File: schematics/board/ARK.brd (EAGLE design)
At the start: 82 x 92 mm, 85 parts, among them IC2 STM32F103C8T

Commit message: Готова схема платы АРК
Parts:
- removed 3,3µH: 3,3µ, CanCubeSat:B82472G6
- removed 3,3µH1: 3,3µH, CanCubeSat:B82472G6
- removed AD5272#2: AD5272, CanCubeSat:MSOP10
- removed C29: 1µ, rcl:C0603
- removed C3: 470nF, rcl:C0603
- removed C40, C41, C49, C50, C56: 0,1µ, rcl:C0603
- removed C44, C52: 680p, rcl:C0603
- removed C45, C53: 4.7µ, rcl:C1206
- removed C46: 3,3n, rcl:C0603
- removed C47, C54: 150µ, CanCubeSat:ECAP150-CMD
- removed C48, C55: 220µ, CanCubeSat:ECAP220-CMD
- removed C57: 10µ, rcl:C1206
- removed INVERT: INVERTER., CanCubeSat:SC70
- removed LED_G1, LED_G2, LED_R1, LED_R2: (no value), led:CHIPLED_0603
- removed OPA: OPA333, CanCubeSat:SOT23-5
- removed R1: 91K, resistor:R0603
- removed R100, R32, R33, R57: 2k, resistor:R0603
- removed R28, R30, R67, R68, R69: 150k, resistor:R0603
- removed R3: 14K3, resistor:R0603
- removed R4: 120k, resistor:R0603
- removed R5: 430k, resistor:R0603
- removed R65: 1M, resistor:R0603
- removed R66: 10k, resistor:R0603
- removed R7: 680k, resistor:R0603
- removed REF3033: REF3033, CanCubeSat:SOT23-3
- removed U$1: MF-R400, CanCubeSat:MF-R400
- removed U$23, U$59: LTC31191, CanCubeSat:LTC3119+VIA
- removed VR-FB: 3314G-1-504E, CanCubeSat:TRIM_3314G-1-504E
- removed VR-RUN: 3313J-1-205E, CanCubeSat:TRIM_3313J-1-205E
- added 3362H, 3362H1: 20k, CanCubeSat:TRIM_3362H
- added 3362P, 3362P1, 3362P4: 1k, CanCubeSat:TRIM_3362P-1-502LF
- added 3362P2, 3362P5: 5k, CanCubeSat:TRIM_3362P-1-502LF
- added 3362P3: 500R, CanCubeSat:TRIM_3362P-1-502LF
- added C1.C, C1.D, C2B.C, C2B.D: 100nF, rcl:C0603
- added C2A.C, C2A.D: 22µF, rcl:C1206
- added C3.C, C3.D, C4A.C, C4A.D, C5.C, C5.D: 1µF, rcl:C0603
- added C4B.C, C4B.D: 1000µF, CanCubeSat:ECAP1000-CMD
- added C6.C, C6.D: 10nF, rcl:C0603
- added C7.C, C7.D, C8.C, C8.D: (10nF), rcl:C0603
- added INVERT1: INVERTER., CanCubeSat:SC70
- added L1.C, L1.D: 10µH, CanCubeSat:L_12X12
- added OPA1, OPA2, OPA3: OPA333, CanCubeSat:SOT23-5
- added PB1, PB2, PB3, PB4, PB6, PB7: (no value), led:CHIPLED_0603
- added R1.C, R1.D: 62k, rcl:R0603
- added R10, R12, R14, R15, R2, R21, R25, R29, R31, R34, R35, R36, R37, R38, R39, R40, R41, R42, R45, R48, R49, R6, R8, R9: 10k, resistor:R0603
- added R10.C, R10.D: 11k, rcl:R0603
- added R11: 34k8, resistor:R0603
- added R11.C, R11.D, R12.C, R12.D, R13.C, R13.D, R14.C, R14.D, R15.C, R15.D: 100k, rcl:R0603
- added R13: 91k, resistor:R0603
- added R16, R17, R18, R22, R23, R24, R26, R43: 2k, resistor:R0603
- added R16.C, R16.D, R17.C, R17.D, R2.C, R2.D, R6.C, R6.D: 10k, rcl:R0603
- added R18.C, R18.D: 51k, rcl:R0603
- added R19, R20: 51k, resistor:R0603
- added R19.C, R19.D: (1M), rcl:R0603
- added R44: 1k, resistor:R0603
- added R46: 24k9, resistor:R0603
- added R47: 620k, resistor:R0603
- added R5.C, R5.D: 191k, rcl:R0603
- added R7.C, R7.D: 17k8, rcl:R0603
- added R8.C, R8.D: (10k), rcl:R0603
- added R9.C, R9.D: 200k, rcl:R0603
- added ROZE1, ROZE2, ROZE3, ROZE4: (no value), pinheadCS:1X02
- added U$10, U$11, U$17, U$18, U$19, U$22, U$24, U$25, U$27, U$28, U$30, U$31, U$32, U$33, U$41, U$42, U$43, U$46, U$47, U$48, U$50, U$51, U$53, U$9: VIAS, CanCubeSat:VIAS
- added U$13, U$14, U$15, U$16, U$20, U$21, U$26, U$29, U$39, U$40, U$44, U$45, U$49, U$52: VIAS-CONNECT, CanCubeSat:VIAS-CONNECT
- added U$2, U$5: MP5515, CanCubeSat:QFN-30
- added U$34, U$35, U$6: IRF7329PBF, CanCubeSat:SO8
- added U$36, U$37: IRF7905PBF, CanCubeSat:SO8
- added U$38: SI2302CDS, CanCubeSat:SOT23-3
- added U$7, U$8: SMP100LC-8, CanCubeSat:SMB
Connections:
- removed net 3V3-STAB: IC2.9, INVERT.P$5, OPA.P$5, R4.1, REF3033.2
- removed net 90: R65.1, R66.2, R67.2, U$59.15
- removed net DPD_RST: AD5272#2.7, IC2.28
- removed net GND-OUT: JP1.11, JP1.12, U$1.P$2, U$12.P$3, U$12.P$5, U$12.P$7, U$12.P$9
- removed net N$129: C41.2, U$59.3
- removed net N$131: 3,3µH.2, C40.1, U$59.21, U$59.24
- removed net N$132: 3,3µH.1, C41.1, U$59.5, U$59.8
- removed net N$135: R69.1, U$59.13
- removed net N$136: C44.1, R69.2
- removed net N$139: C46.1, R66.1
- removed net N$142: R68.2, U$59.17
- removed net N$144: C40.2, U$59.26
- removed net N$161: IC2.41, R81.1
- removed net N$2: OPA.P$3, R4.2, R5.2, R7.2
- removed net N$215: AD5272#2.1, C53.1, C56.1, C57.1, LED_G2.A, U$23.11, U$23.15, U$23.16
- removed net N$234: C45.1, LED_G1.A, U$59.11, U$59.16
- removed net N$3: AD5272#2.2, R1.2, U$23.12
- removed net N$48: AD5272#2.3, AD5272#2.4, C29.2, R3.1
- removed net N$51: AD5272#2.5, C29.1
- removed net N$77: 3,3µH1.2, C49.1, U$23.21, U$23.24
- removed net N$78: 3,3µH1.1, C50.1, U$23.5, U$23.8
- removed net N$79: R28.2, U$23.17
- removed net N$80: C49.2, U$23.26
- removed net N$81: R30.1, U$23.13
- removed net N$82: C52.1, R30.2
- removed net N$84: C50.2, U$23.3
- removed net N$85: LED_R1.A, R32.2
- removed net N$87: LED_R2.A, R57.2
- removed net N$89: U$59.12, VR-FB.2
- removed net N$91: LED_G1.C, R100.2
- removed net N$92: LED_G2.C, R33.2
- removed net PGOOD1: IC2.19, LED_R2.C, U$59.10
- removed net PGOOD2: IC2.18, LED_R1.C, U$23.10
- removed net RUN: OPA.P$4, VR-RUN.2
- new net 0V8: 3362P.2, OPA2.P$3, U$32.P$1
- new net AGND: C1.C.1, C1.D.1, C3.C.2, C3.D.2, C6.C.2, C6.D.2, C7.C.2, C7.D.2, C8.C.2, C8.D.2, R10.C.2, R10.D.2, R13.C.1, R13.D.1, R18.C.2, R18.D.2, R19.C.2, R19.D.2, R2.C.2, R2.D.2, R6.C.2, R6.D.2, R7.C.1, R7.D.1, U$2.9, U$39.2, U$5.9
- new net DC-DC: IC2.38, R42.2, U$38.1
- new net FBB-C: R15.2, U$2.22
- new net FBB-D: R25.2, U$5.22
- new net INT-C: IC2.40, R15.C.1, U$2.17
- new net INT-D: IC2.29, R15.D.1, U$5.17
- new net LED: IC2.18, R81.1
- new net N$10: R1.C.2, R2.C.1, U$2.10
- new net N$100: 3362P5.2, OPA1.P$4, U$48.P$1
- new net N$101: R45.2, U$44.1, U$47.P$1
- new net N$102: R46.1, U$45.2, U$46.P$1
- new net N$104: 3362H1.1, R48.1
- new net N$105: 3362H1.2, OPA1.P$3, U$51.P$1
- new net N$106: 3362H1.3, R47.2
- new net N$108: R47.1, U$49.2, U$50.P$1
- new net N$109: R48.2, U$52.2, U$53.P$1
- new net N$11: R10.C.1, R9.C.2, U$2.4
- new net N$12: C8.C.1, U$2.7
- new net N$13: R18.C.1, U$2.21
- new net N$15: R19.C.1, U$2.20
- new net N$16: R13.C.2, U$2.5
- new net N$18: C6.C.1, U$2.1
- new net N$19: C4A.C.2, C4B.C.P$1, R5.C.1, R8.C.1, U$2.26
- new net N$20: C5.C.2, U$2.25
- new net N$21: C5.C.1, L1.C.P$1, U$2.27
- new net N$22: R5.C.2, R6.C.1, U$2.23
- new net N$23: R8.C.2, U$2.24
- new net N$24: 3362P4.1, R22.1
- new net N$25: R29.2, U$36.7, U$36.8, U$6.4
- new net N$26: R17.C.1, U$2.19
- new net N$27: R16.C.1, U$2.18
- new net N$28: R35.2, U$34.2, U$37.5, U$37.6
- new net N$29: 3362P2.2, OPA3.P$3, U$19.P$1
- new net N$30: R11.D.1, R12.D.2, U$5.13
- new net N$31: R1.D.2, R2.D.1, U$5.10
- new net N$32: R10.D.1, R9.D.2, U$5.4
- new net N$33: R7.D.2, U$5.8
- new net N$34: C7.D.1, U$5.3
- new net N$35: C8.D.1, U$5.7
- new net N$36: R18.D.1, U$5.21
- new net N$37: R19.D.1, U$5.20
- new net N$38: R13.D.2, U$5.5
- new net N$39: C6.D.1, U$5.1
- new net N$40: C5.D.2, U$5.25
- new net N$41: C5.D.1, L1.D.P$1, U$5.27
- new net N$42: R5.D.2, R6.D.1, U$5.23
- new net N$43: R8.D.2, U$5.24
- new net N$44: C4A.D.2, C4B.D.P$1, R5.D.1, R8.D.1, U$5.26
- new net N$46: U$35.5, U$35.6, U$35.7, U$35.8
- new net N$47: R17.D.1, U$5.19
- new net N$49: R16.D.1, U$5.18
- new net N$5: R34.2, U$34.4, U$37.7, U$37.8
- new net N$52: OPA2.P$1, R15.1, U$29.1
- new net N$53: 3362H.2, OPA2.P$4, U$28.P$1
- new net N$54: 3362H.3, R9.2
- new net N$55: 3362H.1, R10.1
- new net N$56: PB1.C, R16.2
- new net N$57: 3362P.3, R11.1
- new net N$58: 3362P.1, R12.2
- new net N$59: 3362P1.3, R13.1
- new net N$6: OPA3.P$1, R25.1, U$13.1
- new net N$60: 3362P1.1, R14.2
- new net N$61: 3362P1.2, U$25.P$1, U$26.1
- new net N$62: 3362P2.3, R20.1
- new net N$63: PB2.C, R17.2
- new net N$64: 3362P2.1, R21.2
- new net N$65: PB3.C, R18.2
- new net N$66: 3362P4.2, OPA3.P$4, U$10.P$1
- new net N$67: 3362P4.3, R19.2
- new net N$68: PB4.C, R23.2
- new net N$69: PB6.C, R24.2
- new net N$7: R11.C.1, R12.C.2, U$2.13
- new net N$70: PB7.C, R26.2
- new net N$71: R22.2, U$13.2, U$9.P$1
- new net N$72: R19.1, U$11.P$1, U$14.2
- new net N$73: R20.2, U$15.1, U$18.P$1
- new net N$74: R21.1, U$16.2, U$17.P$1
- new net N$75: R13.2, U$21.2, U$24.P$1
- new net N$76: R14.1, U$20.1, U$22.P$1
- new net N$8: R7.C.2, U$2.8
- new net N$83: R9.1, U$26.2, U$27.P$1
- new net N$86: R10.2, U$29.2, U$30.P$1
- new net N$88: R31.2, U$36.5, U$36.6, U$6.2
- new net N$9: C7.C.1, U$2.3
- new net N$90: 3362P3.3, R43.1
- new net N$93: 3362P3.1, R44.2
- new net N$94: 3362P3.2, U$43.P$1, U$52.1
- new net N$95: R40.2, R41.2, U$35.2, U$35.4, U$38.3
- new net N$96: R43.2, U$39.1, U$42.P$1
- new net N$97: R44.1, U$40.2, U$41.P$1
- new net N$98: 3362P5.3, R45.1
- new net N$99: 3362P5.1, R46.2
- new net PFI-C: IC2.42, PB1.A, R14.C.2, U$2.6
- new net PFI-D: IC2.27, PB4.A, R14.D.2, U$5.6
- new net PGB-C: IC2.43, PB3.A, U$2.16
- new net PGB-D: IC2.28, PB7.A, U$5.16
- new net PGS-C: IC2.41, PB2.A, U$2.15
- new net PGS-D: IC2.26, PB6.A, U$5.15
- new net ROZE-1: IC2.17, R2.1, ROZE1.1
- new net ROZE-2: IC2.39, R6.1, ROZE2.1
- new net ROZE-3: IC2.32, R8.1, ROZE3.1
- new net ROZE-4: IC2.19, R49.1, ROZE4.1
- new net VB-C: C2A.C.1, C2B.C.1, R12.C.1, R31.1, U$2.12, U$2.29, U$6.1
- new net VB-D: C2A.D.1, C2B.D.1, R12.D.1, R35.1, U$34.1, U$5.12, U$5.29
- new net VBO-C: L1.C.P$2, U$2.14
- new net VBO-D: L1.D.P$2, U$5.14
- new net VCC-C: C3.C.1, R14.C.1, R15.C.2, R16.C.2, R17.C.2, U$2.2
- new net VCC-D: C3.D.1, R14.D.1, R15.D.2, R16.D.2, R17.D.2, U$5.2
- new net VIN-C: C1.C.2, R1.C.1, R11.C.2, R9.C.1, U$2.11, U$2.30, U$6.7, U$6.8, U$7.P$2
- new net VIN-D: C1.D.2, R1.D.1, R11.D.2, R9.D.1, U$34.7, U$34.8, U$5.11, U$5.30, U$8.P$2
- net 1W: now also IC2.15; no longer IC2.17
- net 3V3: now also IC2.9, INVERT1.P$5, OPA1.P$5, OPA2.P$5, OPA3.P$5, R11.2, R2.2, R49.2, R6.2, R8.2, U$31.P$1, U$40.1
- net A: now also INVERT1.P$2, OPA1.P$1, R38.2, R39.2, U$37.2, U$37.4, U$49.1; no longer INVERT.P$2, OPA.P$1, R32.1, R7.1, U$23.18
- net BMS+: now also R34.1, R40.1, U$14.1, U$34.3, U$35.3, U$6.5, U$6.6; no longer C3.2, REF3033.1
- net BMS1: now also IC2.11; no longer IC2.16
- net BMS2: now also IC2.12; no longer IC2.15
- net BMS3: now also IC2.4; no longer IC2.14
- net BMS4: now also IC2.10; no longer IC2.13
- net BMS5: now also IC2.2; no longer IC2.12
- net BMS6: now also IC2.3; no longer IC2.11
- net BUS+: now also R29.1, R41.1, U$15.2, U$21.1, U$34.5, U$34.6, U$35.1, U$45.1, U$6.3
- net GND: now also C2A.C.2, C2A.D.2, C2B.C.2, C2B.D.2, C4A.C.1, C4A.D.1, C4B.C.P$2, C4B.D.P$2, INVERT1.P$3, JP1.11, JP1.12, OPA1.P$2, OPA2.P$2, OPA3.P$2, R12.1, R16.1, R17.1, R18.1, R23.1, R24.1, R26.1, R36.1, R37.1, R38.1, R39.1, R42.1, ROZE1.2, ROZE2.2, ROZE3.2, ROZE4.2, U$12.P$3, U$12.P$5, U$12.P$7, U$12.P$9, U$16.1, U$20.2, U$33.P$1, U$36.1, U$36.3, U$37.1, U$37.3, U$38.2, U$44.2, U$7.P$1, U$8.P$1; no longer AD5272#2.10, AD5272#2.6, C3.1, C44.2, C45.2, C46.2, C47.P$2, C48.P$2, C52.2, C53.2, C54.P$2, C55.P$2, C56.2, C57.2, IC2.20, INVERT.P$3, OPA.P$2, R100.1, R28.1, R3.2, R33.1, R5.1, R67.1, R68.1, REF3033.3, U$1.P$1, U$23.14, U$23.20, U$23.25, U$23.28, U$23.29, U$23.4, U$23.9, U$23.P$1, U$23.P$10, U$23.P$2, U$23.P$3, U$23.P$4, U$23.P$5, U$23.P$6, U$23.P$7, U$23.P$8, U$23.P$9, U$59.14, U$59.20, U$59.25, U$59.28, U$59.29, U$59.4, U$59.9, U$59.P$1, U$59.P$10, U$59.P$2, U$59.P$3, U$59.P$4, U$59.P$5, U$59.P$6, U$59.P$7, U$59.P$8, U$59.P$9, VR-FB.3, VR-RUN.3
- net INA_BMS+: no longer C47.P$1, C55.P$1, U$23.19, U$23.22, U$23.23, U$59.6, U$59.7, VR-FB.1
- net INA_BUS+: no longer C48.P$1, C54.P$1, R1.1, R65.2, U$23.6, U$23.7, U$59.19, U$59.22, U$59.23, VR-RUN.1
- net SCL: no longer AD5272#2.9
- net SDA: no longer AD5272#2.8
- net TIME: now also IC2.13; no longer IC2.42
- net Y: now also INVERT1.P$4, R36.2, R37.2, U$36.2, U$36.4; no longer INVERT.P$4, R57.1, U$59.18
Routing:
- net GND-OUT: track 188.6 -> 0.00 mm
- net 3V3-STAB: track 145.8 -> 0.00 mm, vias 2 -> 0
- net 3V3: track 202.4 -> 330.5 mm, vias 19 -> 21
- net Y: track 83.6 -> 0.00 mm, vias 5 -> 0
- net PGOOD2: track 82.1 -> 0.00 mm, vias 5 -> 0
- net PGOOD1: track 76.9 -> 0.00 mm, vias 5 -> 0
- net A: track 61.1 -> 0.00 mm, vias 4 -> 0
- net DPD_RST: track 57.6 -> 0.00 mm, vias 2 -> 0
- net RUN: track 57.4 -> 0.00 mm, vias 2 -> 0
- net N$215: track 43.7 -> 0.00 mm, vias 4 -> 0
- net N$234: track 41.6 -> 0.00 mm, vias 3 -> 0
- net GND: track 486.6 -> 449.6 mm, vias 20 -> 18
- net INA_BUS+: track 132.9 -> 101.4 mm, vias 5 -> 2
- net N$3: track 30.7 -> 0.00 mm
- net INA_BMS+: track 121.2 -> 92.6 mm, vias 4 -> 2
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- removed copper zone on layer 16, net GND-OUT

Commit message: Начата разводка платы АРК
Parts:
- C4A.C, C4A.D: device rcl:C0603 -> rcl:C1206
- moved R49 835.2 mm to (3.25, 47.8), turned to 180 degrees
- moved R8 827.0 mm to (3.25, 50.0), turned to 180 degrees
- moved R6 818.9 mm to (3.25, 52.2), turned to 180 degrees
- moved ROZE4 812.9 mm to (2.75, 29.5), turned to 270 degrees
- moved R2 810.7 mm to (3.25, 54.5), turned to 180 degrees
- moved ROZE3 796.1 mm to (2.75, 23.0), turned to 270 degrees
- moved ROZE2 779.3 mm to (2.75, 16.5), turned to 270 degrees
- moved U$51 754.8 mm to (118.5, -4.25)
- moved U$52 751.9 mm to (114.0, -4.25)
- moved R48 751.2 mm to (113.5, -1.50), turned to 270 degrees
- moved U$53 751.0 mm to (116.0, -4.25)
- moved U$49 750.0 mm to (123.0, -4.25), turned to 180 degrees
- moved U$50 747.9 mm to (121.0, -4.25)
- moved ROZE1 746.2 mm to (2.75, 10.0), turned to 270 degrees
- moved 3362H1 745.7 mm to (118.5, 0.50)
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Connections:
- new net N$2: IC2.19
- new net N$3: IC2.20
- net 1W: now also IC2.14; no longer IC2.15
- net AGND: no longer C1.C.1, C1.D.1
- net BMS+: no longer R34.1, R40.1, U$34.3, U$35.3, U$6.5, U$6.6
- net BUS+: no longer R29.1, R41.1, U$34.5, U$34.6, U$35.1, U$6.3
- net GND: now also C1.C.1, C1.D.1, U$2.28, U$5.28
- net INA_BMS+: now also R34.1, R40.1, U$34.3, U$35.3, U$6.5, U$6.6
- net INA_BUS+: now also R29.1, R41.1, U$34.5, U$34.6, U$35.1, U$6.3
- net INT-C: now also IC2.26; no longer IC2.40
- net INT-D: now also IC2.40; no longer IC2.29
- net LED: now also IC2.25; no longer IC2.18
- net PFI-C: now also IC2.29; no longer IC2.42
- net PFI-D: now also IC2.43; no longer IC2.27
- net PGB-C: now also IC2.27; no longer IC2.43
- net PGB-D: now also IC2.42; no longer IC2.28
- net PGS-C: now also IC2.28; no longer IC2.41
- net PGS-D: now also IC2.41; no longer IC2.26
- net ROZE-1: now also IC2.15; no longer IC2.17
- net ROZE-2: now also IC2.16; no longer IC2.39
- net ROZE-3: now also IC2.17; no longer IC2.32
- net ROZE-4: now also IC2.18; no longer IC2.19
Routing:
- net 3V3: track 330.5 -> 115.1 mm, vias 21 -> 12
- net GND: track 449.6 -> 247.9 mm, vias 18 -> 125
- net BMS+: track 143.9 -> 38.5 mm
- net SDATM: track 79.2 -> 0.00 mm, vias 3 -> 0
- net SCLTM: track 77.3 -> 0.00 mm, vias 3 -> 0
- net TIME: track 73.4 -> 0.00 mm, vias 3 -> 0
- net SDA: track 77.7 -> 15.4 mm, vias 3 -> 1
- net SCL: track 74.3 -> 12.8 mm, vias 3 -> 1
- net NRST: track 67.2 -> 6.35 mm
- net BMS6: track 59.2 -> 0.00 mm, vias 1 -> 0
- net BMS2: track 57.3 -> 0.00 mm, vias 1 -> 0
- net BMS4: track 56.7 -> 0.00 mm, vias 1 -> 0
- net BMS5: track 56.0 -> 0.00 mm, vias 1 -> 0
- net BMS1: track 54.6 -> 0.00 mm, vias 1 -> 0
- net BMS3: track 54.0 -> 0.00 mm, vias 1 -> 0
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- added copper zone on layer 1, net AGND
- added copper zone on layer 1, net N$19
- added copper zone on layer 1, net N$21
- added copper zone on layer 1, net N$41
- added copper zone on layer 1, net N$44
- added copper zone on layer 1, net VB-C
- added copper zone on layer 1, net VB-D
- added copper zone on layer 1, net VBO-C
- added copper zone on layer 1, net VBO-D
- added copper zone on layer 1, net VCC-C
- added copper zone on layer 1, net VCC-D
- added copper zone on layer 1, net VIN-C
- added copper zone on layer 1, net VIN-D
- removed copper zone on layer 1, net INA_BMS+
- removed copper zone on layer 16, net INA_BMS+
- removed copper zone on layer 1, net INA_BUS+
- removed copper zone on layer 16, net INA_BUS+
- removed copper zone on layer 1, net N$131
- removed copper zone on layer 1, net N$132
- removed copper zone on layer 1, net N$215
- removed copper zone on layer 1, net N$234
- removed copper zone on layer 1, net N$77
- removed copper zone on layer 1, net N$78
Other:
- outline, holes or cut-outs redrawn
- board text removed: "BMS+"

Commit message: Разведена плата АРК
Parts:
- removed C15: 100nF, rcl:C0603
- removed R36, R37: 10k, resistor:R0603
- added R1: 10k, resistor:R0603
- added R3: 100, resistor:R0603
- R39: value 10k -> 100
- moved U$3 111.3 mm to (51.2, 82.2)
- moved R46 111.0 mm to (31.2, 41.2), turned to 180 degrees
- moved U$45 106.4 mm to (38.0, 40.0), turned to 270 degrees
- moved U$46 103.8 mm to (38.0, 38.2), turned to 0 degrees
- moved 3362P5 103.4 mm to (33.2, 36.2), turned to 270 degrees
- moved U$48 100.7 mm to (38.0, 36.2), turned to 0 degrees
- moved R45 98.3 mm to (31.2, 31.2), turned to 0 degrees
- moved U$47 97.7 mm to (38.0, 34.2), turned to 0 degrees
- moved U$44 95.1 mm to (38.0, 32.5), turned to 270 degrees
- moved R47 94.1 mm to (35.2, 31.2), turned to 180 degrees
- moved U$49 91.6 mm to (38.0, 30.0), turned to 270 degrees
- moved U$50 89.1 mm to (38.0, 28.2), turned to 90 degrees
- moved 3362H1 89.1 mm to (33.2, 26.2), turned to 90 degrees
- moved U$51 86.1 mm to (38.0, 26.2), turned to 90 degrees
- moved U$53 83.0 mm to (38.0, 24.2), turned to 90 degrees
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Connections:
- removed net N$2: IC2.19
- removed net N$3: IC2.20
- new net C-OFF: IC2.19, R3.1
- new net D-OFF: IC2.20, R39.2
- new net N$48: R1.2, R3.2, U$36.2, U$36.4
- new net N$51: R38.1, R39.1, U$37.2, U$37.4
- net 3V3: no longer C15.1
- net A: no longer R39.2, U$37.2, U$37.4
- net AGND: now also INVERT1.P$3, OPA1.P$2, OPA2.P$2, OPA3.P$2
- net GND: no longer C15.2, INVERT1.P$3, OPA1.P$2, OPA2.P$2, OPA3.P$2, R36.1, R37.1, R38.1, R39.1
- net INA_BMS+: now also U$6.7, U$6.8; no longer U$6.5, U$6.6
- net INA_BUS+: now also U$34.7, U$34.8; no longer U$34.5, U$34.6
- net INT-D: now also IC2.41; no longer IC2.40
- net N$25: now also U$36.5, U$36.6; no longer U$36.7, U$36.8
- net N$28: now also U$37.7, U$37.8; no longer U$37.5, U$37.6
- net N$5: now also U$37.5, U$37.6; no longer U$37.7, U$37.8
- net N$88: now also U$36.7, U$36.8; no longer U$36.5, U$36.6
- net PFI-D: now also IC2.40; no longer IC2.43
- net PGS-D: now also IC2.43; no longer IC2.41
- net VIN-C: now also U$6.5, U$6.6; no longer U$6.7, U$6.8
- net VIN-D: now also U$34.5, U$34.6; no longer U$34.7, U$34.8
- net Y: now also R1.1; no longer R36.2, R37.2, U$36.2, U$36.4
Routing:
- net 3V3: track 115.1 -> 369.9 mm, vias 12 -> 17
- net BUS+: track 35.7 -> 170.8 mm, vias 2 -> 12
- net PFI-C: track 22.2 -> 136.1 mm, vias 2 -> 4
- net PGS-C: track 0.00 -> 98.7 mm, vias 0 -> 4
- net PGS-D: track 0.00 -> 97.9 mm, vias 0 -> 2
- net PGB-C: track 0.00 -> 97.0 mm, vias 0 -> 4
- net PGB-D: track 0.00 -> 92.8 mm, vias 0 -> 2
- net INA_BUS+: track 78.2 -> 160.3 mm
- net FBB-D: track 0.00 -> 79.0 mm, vias 0 -> 2
- net INT-C: track 24.6 -> 103.3 mm, vias 2 -> 4
- net INA_BMS+: track 95.1 -> 171.3 mm
- net TIME: track 0.00 -> 74.9 mm
- net INT-D: track 24.1 -> 95.5 mm
- net FBB-C: track 0.00 -> 71.0 mm, vias 0 -> 2
- net SCLTM: track 0.00 -> 66.3 mm, vias 0 -> 2
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- added copper zone on layer 1, net 3V3
- added copper zone on layer 16, net 3V3
- added copper zone on layer 16, net AGND
- added copper zone on layer 16, net BMS+
- added copper zone on layer 16, net BUS+
- added copper zone on layer 1, net INA_BMS+
- added copper zone on layer 1, net INA_BUS+
- added copper zone on layer 16, net VB-C
- added copper zone on layer 16, net VB-D
- added copper zone on layer 16, net VCC-C
- added copper zone on layer 16, net VCC-D
- added copper zone on layer 16, net VIN-C
- added copper zone on layer 16, net VIN-D

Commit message: Плата АРК готова
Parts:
- removed 3362H, 3362H1: 20k, CanCubeSat:TRIM_3362H
- removed PB1, PB2, PB3, PB4, PB5, PB6, PB7: (no value), led:CHIPLED_0603
- added 3362P6, 3362P7: 20k, CanCubeSat:TRIM_3362P-1-502LF
- added LED, PFI-C, PFI-D, PGB-C, PGB-D, PGS-C, PGS-D: (no value), led:CHIPLED_0603
- added R28, R4, R5, R7: 100, resistor:R0603
- added U$1: VIN-C, CanCubeSat:SOLDERING-PAD-4A
- added U$23: VB-C, CanCubeSat:SOLDERING-PAD-4A
- added U$54: VIN-D, CanCubeSat:SOLDERING-PAD-4A
- added U$55: VB-D, CanCubeSat:SOLDERING-PAD-4A
- U$10, U$28, U$48: value VIAS -> IN-
- U$11, U$17, U$18, U$22, U$24, U$27, U$30, U$41, U$42, U$46, U$47, U$50, U$53, U$9: value VIAS -> (none)
- U$13, U$29: value VIAS-CONNECT -> OUT
- U$14: value VIAS-CONNECT -> BMS+
- U$15, U$21, U$45: value VIAS-CONNECT -> BUS+
- U$16, U$20, U$39, U$44: value VIAS-CONNECT -> AGND
- U$19, U$32, U$51: value VIAS -> IN+
- U$25, U$43: value VIAS -> REF
- U$26, U$52: value VIAS-CONNECT -> REF
- U$31: value VIAS -> 3V3
- U$33: value VIAS -> AGND
- U$40: value VIAS-CONNECT -> 3V3
- U$49: value VIAS-CONNECT -> OUT-D
- moved U$4 67.5 mm to (27.5, 8.25)
- moved R24 6.00 mm to (21.0, 60.8)
- moved R26 4.75 mm to (21.0, 57.2)
- moved R23 3.50 mm to (21.0, 53.8)
- moved U$36 2.25 mm to (74.5, 42.0)
- moved U$37 2.25 mm to (46.5, 49.8)
- moved R18 1.75 mm to (21.0, 11.0)
- moved U$3 1.25 mm to (51.2, 83.5)
- moved R16 0.75 mm to (21.0, 18.0)
- moved R17 0.50 mm to (21.0, 14.5)
- moved PWR 0.10 mm to (22.0, 30.0)
- moved R31 0.10 mm to (66.5, 40.4)
- renumbered U$7 to D$1, U$8 to D$2
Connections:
- new net N$2: U$1.P$1, U$6.5, U$6.6
- new net N$3: R31.1, U$23.P$1, U$6.1
- new net N$50: U$34.5, U$34.6, U$54.P$1
- new net N$77: R35.1, U$34.1, U$55.P$1
- new net N$78: R5.2, U$37.7, U$37.8
- new net N$79: R28.1, U$36.7, U$36.8
- new net N$80: R4.2, U$37.5, U$37.6
- new net N$81: R7.1, U$36.5, U$36.6
- net 3V3: now also LED.A; no longer PB5.A
- net AGND: now also R12.1, U$16.1, U$20.2, U$33.P$1, U$44.2
- net GND: no longer R12.1, U$16.1, U$20.2, U$33.P$1, U$44.2
- net N$104: now also 3362P7.1; no longer 3362H1.1
- net N$105: now also 3362P7.2; no longer 3362H1.2
- net N$106: now also 3362P7.3; no longer 3362H1.3
- net N$17: now also LED.C; no longer PB5.C
- net N$25: now also R7.2; no longer U$36.5, U$36.6
- net N$28: now also R5.1; no longer U$37.7, U$37.8
- net N$5: now also R4.1; no longer U$37.5, U$37.6
- net N$53: now also 3362P6.2; no longer 3362H.2
- net N$54: now also 3362P6.3; no longer 3362H.3
- net N$55: now also 3362P6.1; no longer 3362H.1
- net N$56: now also PFI-C.C; no longer PB1.C
- net N$63: now also PGS-C.C; no longer PB2.C
- net N$65: now also PGB-C.C; no longer PB3.C
- net N$68: now also PFI-D.C; no longer PB4.C
- net N$69: now also PGS-D.C; no longer PB6.C
- net N$70: now also PGB-D.C; no longer PB7.C
- net N$88: now also R28.2; no longer U$36.7, U$36.8
- net PFI-C: now also PFI-C.A; no longer PB1.A
- net PFI-D: now also PFI-D.A; no longer PB4.A
- net PGB-C: now also PGB-C.A; no longer PB3.A
- net PGB-D: now also PGB-D.A; no longer PB7.A
- net PGS-C: now also PGS-C.A; no longer PB2.A
- net PGS-D: now also PGS-D.A; no longer PB6.A
- net VB-C: now also U$23.P$2; no longer R31.1, U$6.1
- net VB-D: now also U$55.P$2; no longer R35.1, U$34.1
- net VIN-C: now also U$1.P$2; no longer U$6.5, U$6.6
- net VIN-D: now also U$54.P$2; no longer U$34.5, U$34.6
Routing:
- net GND: track 245.9 -> 198.4 mm
- net VIN-C: track 42.2 -> 29.7 mm, vias 15 -> 11
- net 3V3: track 369.9 -> 382.1 mm
- net AGND: track 48.4 -> 59.7 mm, vias 79 -> 82
- net VIN-D: track 43.5 -> 32.6 mm, vias 15 -> 11
- net PGS-D: track 97.9 -> 106.6 mm
- net N$2: track 0.00 -> 8.45 mm, vias 0 -> 4
- net N$50: track 0.00 -> 7.31 mm, vias 0 -> 4
- net VB-D: track 29.3 -> 22.2 mm, vias 15 -> 11
- net PGB-D: track 92.8 -> 99.8 mm
- net VB-C: track 29.1 -> 22.1 mm, vias 15 -> 11
- net N$77: track 0.00 -> 6.21 mm, vias 0 -> 4
- net N$3: track 0.00 -> 6.17 mm, vias 0 -> 4
- net INT-D: track 95.5 -> 100.4 mm
- net N$78: track 0.00 -> 4.23 mm
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- added copper zone on layer 1, net N$2
- added copper zone on layer 16, net N$2
- added copper zone on layer 1, net N$3
- added copper zone on layer 16, net N$3
- added copper zone on layer 1, net N$50
- added copper zone on layer 16, net N$50
- added copper zone on layer 1, net N$77
- added copper zone on layer 16, net N$77
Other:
- board text added: "DC-DC`s CONTROL"
- board text added: "FBB-C"
- board text added: "FBB-D"
- board text removed: "ERR"
- board text removed: "ON"

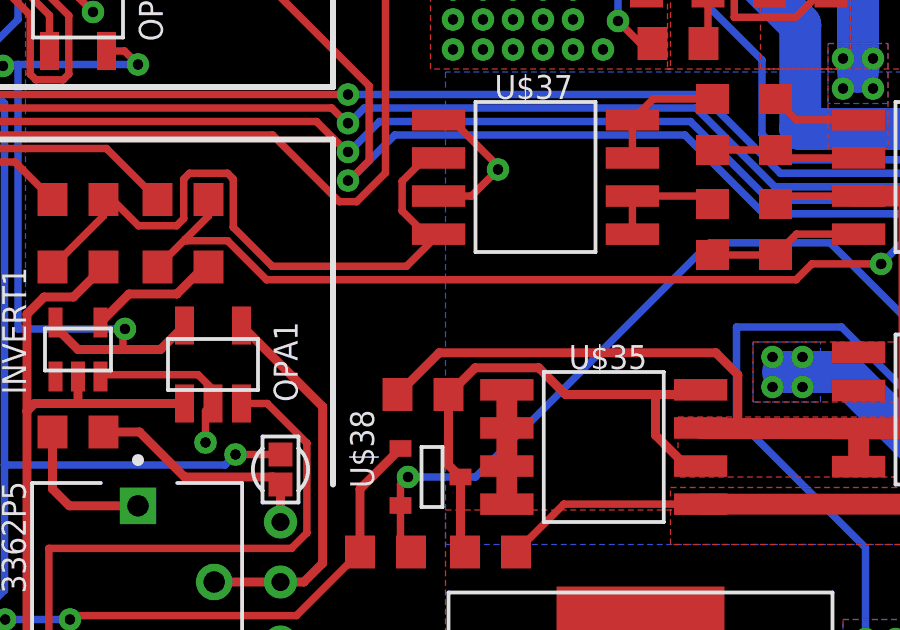
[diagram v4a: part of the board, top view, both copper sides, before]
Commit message: Забыл объединить земли на плате АРК. Исправился
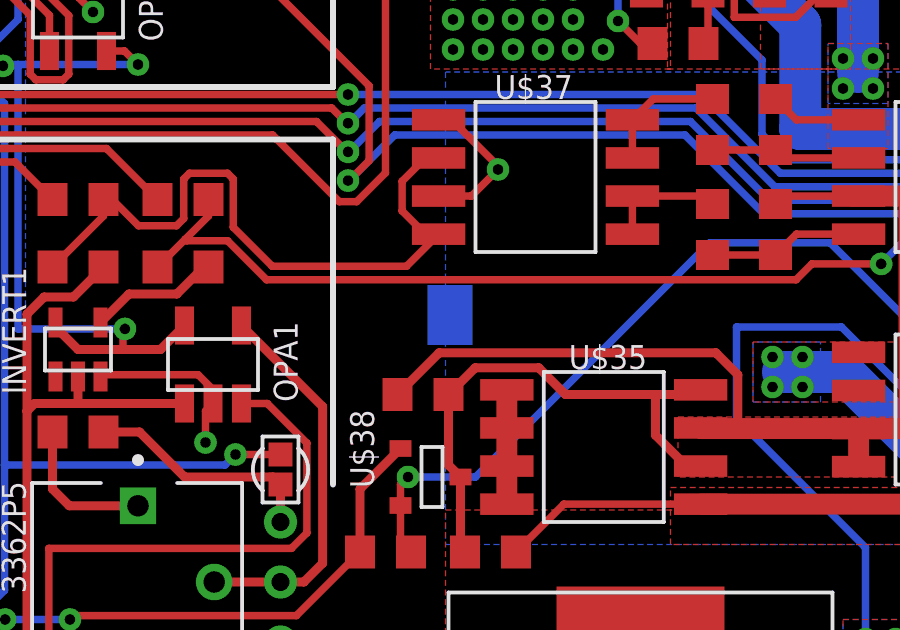
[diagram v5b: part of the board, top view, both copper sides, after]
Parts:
- added U$7: GNDS-CONNECTOR, CanCubeSat:GNDS-CONNECTOR
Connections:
- net AGND: now also U$7.P$2
- net GND: now also U$7.P$1
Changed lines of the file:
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@@
 <layer number="28" name="bValues" color="7" fill="1" visible="no" active="yes"/>
 <layer number="29" name="tStop" color="7" fill="3" visible="no" active="yes"/>
-<layer number="30" name="bStop" color="7" fill="6" visible="no" active="yes"/>
+<layer number="30" name="bStop" color="7" fill="6" visible="yes" active="yes"/>
 <layer number="31" name="tCream" color="7" fill="4" visible="no" active="yes"/>
 <layer number="32" name="bCream" color="7" fill="5" visible="no" active="yes"/>
@@
 <attribute name="VALUE" x="29.56216875" y="23.14258125" size="0.8" layer="27" ratio="15" rot="R90"/>
 </element>
+<element name="U$7" library="CanCubeSat" package="GNDS-CONNECTOR" value="GNDS-CONNECTOR" x="43.65" y="45.15" smashed="yes" rot="MR0"/>
 </elements>
 <signals>
@@
 <wire x1="18.875" y1="55.87101875" x2="20.15" y2="57.14601875" width="0.25" layer="1"/>
 <wire x1="18.875" y1="48.7386" x2="18.875" y2="55.87101875" width="0.25" layer="1"/>
+<contactref element="U$7" pad="P$1"/>
 </signal>
 <signal name="INA_BUS+">
@@
 <wire x1="52.25" y1="2.5" x2="52.25" y2="1.75" width="0.25" layer="1"/>
 <via x="52.25" y="1.75" extent="1-16" drill="0.35"/>
+<contactref element="U$7" pad="P$2"/>
 </signal>
 <signal name="N$7">
@@
 <mfgpreviewcolor name="substratecolor" color="0xFF786E46"/>
 </mfgpreviewcolors>
+<errors>
+</errors>
 </board>
 </drawing>
